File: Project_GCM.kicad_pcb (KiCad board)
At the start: 4 copper layers, 203 x 116 mm, 91 parts, among them IC1 LTC6903CMS8#PBF, J1 Conn_02x04_Odd_Even, J10 Conn_01x10, J11 5530843-2, J12 Conn_02x21_Odd_Even, J13 Conn_01x10, J2 5-5530843-4, J3 5-5530843-4, J4 5-5530843-4, J5 5-5530843-4, J6 TE_Eurocard_96pole, J7 3-641124-6, J8 5530843-2, J9 Conn_01x02, U1 LM810, U10 74LVC1G74, U11 74AHC1G04, U12 74AHC244, U13 SN74LV163A, U14 SN74LV163A, U15 74AHC1G04, U16 SN74LV163A, U17 SN74LV163A, U18 74AHC1G04, U19 SN74LV163A, U2 LTC6994-1, U20 SN74LV163A, U21 74AHC244, U22 74CBTLV16212, U23 74CBTLV16212, U24 74CBTLV16212, U3 74AHC1G32, U4 74AHC273, U5 74AHC1G04, U6 CD74AC238, U7 74AHC138, U8 74AHC244, U9 74AHC244

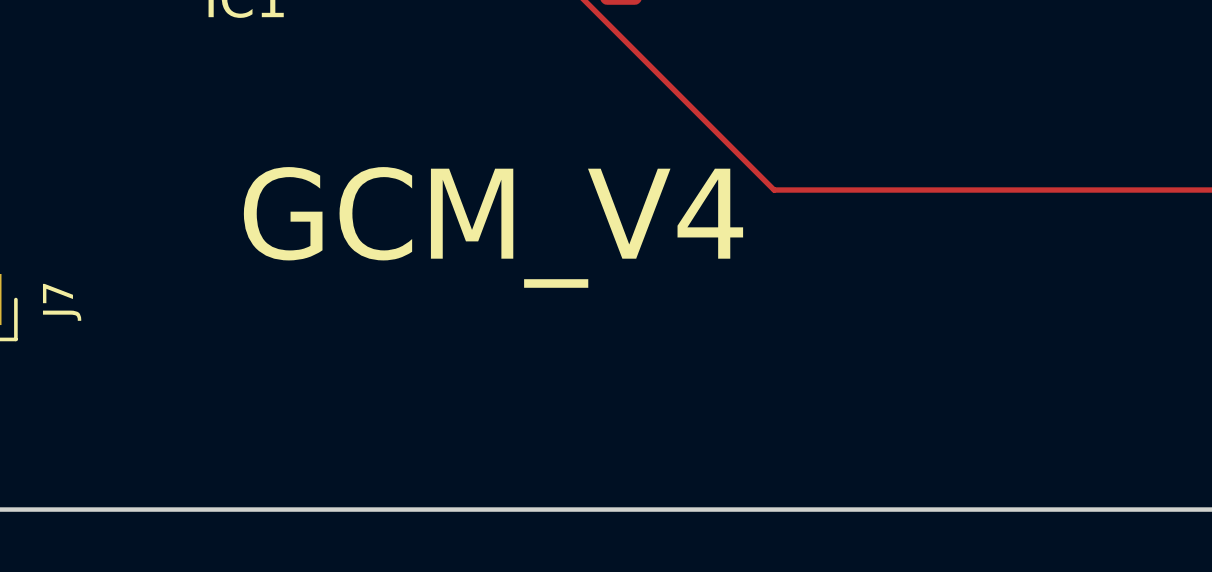
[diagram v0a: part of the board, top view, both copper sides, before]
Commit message: License info on silks
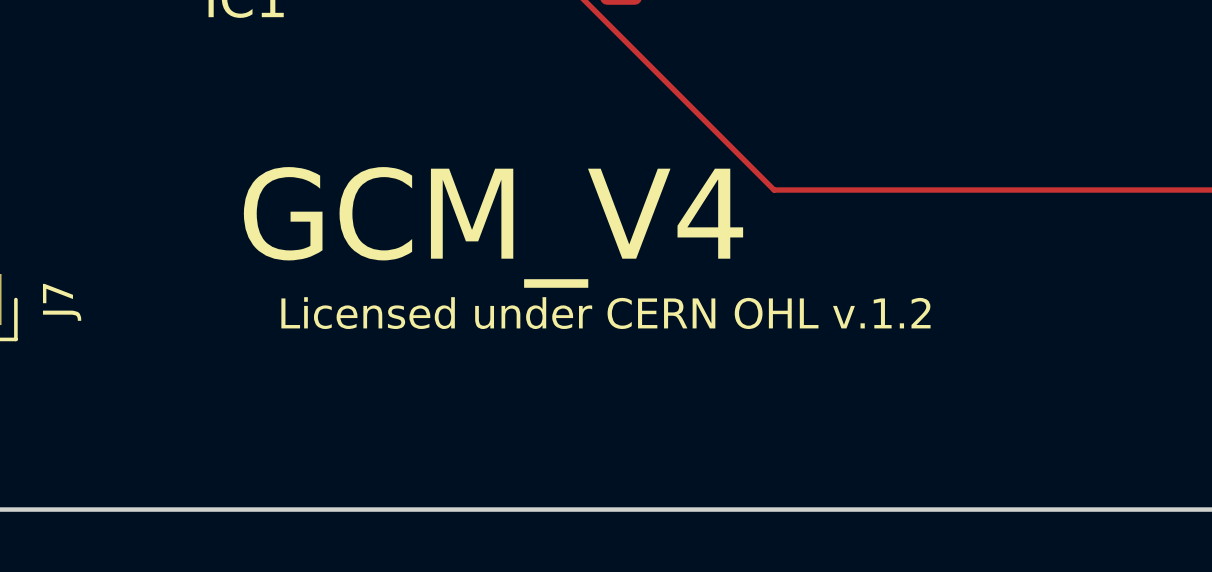
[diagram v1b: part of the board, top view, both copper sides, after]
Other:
- board text added: "Licensed under CERN OHL v.1.2"
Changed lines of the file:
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@@
-(kicad_pcb (version 20171130) (host pcbnew "(5.1.2)-1")
+(kicad_pcb (version 20171130) (host pcbnew "(5.1.4)-1")
   (general
     (thickness 1.6)
-    (drawings 42)
+    (drawings 43)
     (tracks 6223)
     (zones 0)
@@
     )
   )
+  (gr_text "Licensed under CERN OHL v.1.2" (at 167 141.5) (layer F.SilkS)
+    (effects (font (size 1 1) (thickness 0.15)))
+  )
   (gr_line (start 271 32) (end 68 32) (angle 90) (layer Edge.Cuts) (width 0.15))

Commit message: Update materials list, begin to work on pcb
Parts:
- removed IC1: LTC6903CMS8#PBF, SOP65P490X110-8N:SOP65P490X110-8N
- added C35: 10nF, Capacitor_SMD:C_0805_2012Metric, F.Cu at (290.1, 22.9)
- added C36: 10nF, Capacitor_SMD:C_0805_2012Metric, F.Cu at (294.5, 22.9)
- added C37: 10nF, Capacitor_SMD:C_0805_2012Metric, F.Cu at (290.1, 25.9)
- added C38: 10nF, Capacitor_SMD:C_0805_2012Metric, F.Cu at (284.9, 48.5)
- added C39: 10nF, Capacitor_SMD:C_0805_2012Metric, F.Cu at (289.4, 48.5)
- added C40: 10nF, Capacitor_SMD:C_0805_2012Metric, F.Cu at (284.9, 51.5)
- added C41: 10nF, Capacitor_SMD:C_0805_2012Metric, F.Cu at (289.4, 51.5)
- added C49: 10nF, Capacitor_SMD:C_0805_2012Metric, F.Cu at (314.7, 45.6)
- added C50: 10nF, Capacitor_SMD:C_0805_2012Metric, F.Cu at (314.7, 48.6)
- added C51: 10nF, Capacitor_SMD:C_0805_2012Metric, F.Cu at (284.9, 63.9)
- added C52: 10nF, Capacitor_SMD:C_0805_2012Metric, F.Cu at (373.0, 38.2)
- added C53: 10nF, Capacitor_SMD:C_0805_2012Metric, F.Cu at (332.4, 23.0)
- added C54: 10nF, Capacitor_SMD:C_0805_2012Metric, F.Cu at (328.0, 26.0)
- added C55: 10nF, Capacitor_SMD:C_0805_2012Metric, F.Cu at (328.0, 23.0)
- added H1: MountingHole_3mm, MountingHole:MountingHole_3mm, F.Cu at (336.7, 36.4)
- added H2: MountingHole_3mm, MountingHole:MountingHole_3mm, F.Cu at (329.2, 44.0)
- added H3: MountingHole_3mm, MountingHole:MountingHole_3mm, F.Cu at (329.2, 36.4)
- added H4: MountingHole_3mm, MountingHole:MountingHole_3mm, F.Cu at (336.7, 44.0)
- added R6: 10k, Resistor_SMD:R_0805_2012Metric, F.Cu at (294.5, 25.9)
- added U25: 74AHC1G32, Package_TO_SOT_SMD:SOT-23-5, F.Cu at (302.0, 60.2)
- added U26: SN74LV393A, Package_SO:SOIC-14_3.9x8.7mm_P1.27mm, F.Cu at (309.6, 23.7)
- added U27: SN74LV393A, Package_SO:SOIC-14_3.9x8.7mm_P1.27mm, F.Cu at (301.2, 23.7)
- added U28: CD74AC151, Package_SO:SOP-16_3.9x9.9mm_P1.27mm, F.Cu at (301.2, 12.8)
- added U29: CD74AC151, Package_SO:SOP-16_3.9x9.9mm_P1.27mm, F.Cu at (309.8, 12.8)
- added U30: 74AHC1G32, Package_TO_SOT_SMD:SOT-23-5, F.Cu at (285.3, 23.6)
- added U31: CD74AC151, Package_SO:SOP-16_3.9x9.9mm_P1.27mm, F.Cu at (318.3, 12.8)
- added U32: 74AHC273, Package_SO:SOIC-20W_7.5x12.8mm_P1.27mm, F.Cu at (289.2, 39.8)
- added U33: SN74LV393A, Package_SO:SOIC-14_3.9x8.7mm_P1.27mm, F.Cu at (308.3, 49.2)
- added U34: SN74LV393A, Package_SO:SOIC-14_3.9x8.7mm_P1.27mm, F.Cu at (299.8, 49.2)
- added U35: CD74AC151, Package_SO:SOP-16_3.9x9.9mm_P1.27mm, F.Cu at (317.0, 38.4)
- added U36: CD74AC151, Package_SO:SOP-16_3.9x9.9mm_P1.27mm, F.Cu at (308.4, 38.4)
- added U37: CD74AC151, Package_SO:SOP-16_3.9x9.9mm_P1.27mm, F.Cu at (299.9, 38.4)
- added U38: 74AHC1G04, Package_TO_SOT_SMD:SOT-23-5, F.Cu at (290.4, 60.2)
- added U39: 74AHC1G04, Package_TO_SOT_SMD:SOT-23-5, F.Cu at (285.3, 60.2)
- added U40: 74AHC273, Package_SO:SOIC-20W_7.5x12.8mm_P1.27mm, F.Cu at (364.3, 39.5)
- added U41: 74AHC1G04, Package_TO_SOT_SMD:SOT-23-5, F.Cu at (373.4, 34.5)
- added U42: 74AHC273, Package_SO:SOIC-20W_7.5x12.8mm_P1.27mm, F.Cu at (332.2, 14.3)
- added U43: 74AHC273, Package_SO:SOIC-20W_7.5x12.8mm_P1.27mm, F.Cu at (345.1, 14.3)
- added U44: 74AHC273, Package_SO:SOIC-20W_7.5x12.8mm_P1.27mm, F.Cu at (358.0, 14.3)
- added X1: ECS-2200BX-500, Oscillator:Oscillator_DIP-8, F.Cu at (286.0, 18.1)
- C24: value 1uF -> 10nF; footprint Capacitor_SMD:C_1206_3216Metric -> Capacitor_SMD:C_0805_2012Metric
- J1: value Conn_02x04_Odd_Even -> PowerSupply
- J10, J13: value Conn_01x10 -> MM1_addressExtension
- J11, J8: value 5530843-2 -> MM1_receptacle_5530843-2
- J12: value Conn_02x21_Odd_Even -> DEBUG_BUSES
- J2, J3, J4, J5: value 5-5530843-4 -> PP1_receptacle_TE_5-5530843-4; footprint Eurocard:SHDR40W89P485X254_2X20_5740X935X1562P -> TE_5-5530843-4:TE_5-5530843-4
- U1: footprint Package_TO_SOT_SMD:SOT-23_Handsoldering -> Package_TO_SOT_SMD:SOT-23
- U10: footprint Package_SO:VSSOP-8_2.4x2.1mm_P0.5mm -> Package_SO:SSOP-8_2.95x2.8mm_P0.65mm
- U13, U14, U16, U17, U19, U20: value SN74LV163A -> CD74AC161M; footprint Package_SO:SOIC-16_3.9x9.9mm_P1.27mm -> Package_SO:SOP-16_3.9x9.9mm_P1.27mm
- U15: value 74AHC1G04 -> 74AHCT1G04
- U2: value LTC6994-1 -> LTC6994xS6-1; footprint Package_TO_SOT_SMD:SOT-23-6 -> Package_TO_SOT_SMD:TSOT-23-6
- U21: value 74AHC244 -> 74AHCT244
- U6: footprint Package_SO:SOIC-16_3.9x9.9mm_P1.27mm -> Package_SO:SOP-16_3.9x9.9mm_P1.27mm
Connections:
- net /MAIN_RESET renamed /POWER_RESET
- net /MemorySlot1/MEM_ADD_0 renamed /MemorySlot1/MEMADDRESS_0
- net /MemorySlot1/MEM_ADD_1 renamed /MemorySlot1/MEMADDRESS_1
- net /MemorySlot1/MEM_ADD_10 renamed /MemorySlot1/MEMADDRESS_10
- net /MemorySlot1/MEM_ADD_11 renamed /MemorySlot1/MEMADDRESS_11
- net /MemorySlot1/MEM_ADD_12 renamed /MemorySlot1/MEMADDRESS_12
- net /MemorySlot1/MEM_ADD_13 renamed /MemorySlot1/MEMADDRESS_13
- net /MemorySlot1/MEM_ADD_14 renamed /MemorySlot1/MEMADDRESS_14
- net /MemorySlot1/MEM_ADD_15 renamed /MemorySlot1/MEMADDRESS_15
- net /MemorySlot1/MEM_ADD_16 renamed /MemorySlot1/MEMADDRESS_16
- net /MemorySlot1/MEM_ADD_17 renamed /MemorySlot1/MEMADDRESS_17
- net /MemorySlot1/MEM_ADD_18 renamed /MemorySlot1/MEMADDRESS_18
- net /MemorySlot1/MEM_ADD_19 renamed /MemorySlot1/MEMADDRESS_19
- net /MemorySlot1/MEM_ADD_2 renamed /MemorySlot1/MEMADDRESS_2
- net /MemorySlot1/MEM_ADD_20 renamed /MemorySlot1/MEMADDRESS_20
- net /MemorySlot1/MEM_ADD_21 renamed /MemorySlot1/MEMADDRESS_21
- net /MemorySlot1/MEM_ADD_22 renamed /MemorySlot1/MEMADDRESS_22
- net /MemorySlot1/MEM_ADD_23 renamed /MemorySlot1/MEMADDRESS_23
- net /MemorySlot1/MEM_ADD_3 renamed /MemorySlot1/MEMADDRESS_3
- net /MemorySlot1/MEM_ADD_4 renamed /MemorySlot1/MEMADDRESS_4
- net /MemorySlot1/MEM_ADD_5 renamed /MemorySlot1/MEMADDRESS_5
- net /MemorySlot1/MEM_ADD_6 renamed /MemorySlot1/MEMADDRESS_6
- net /MemorySlot1/MEM_ADD_7 renamed /MemorySlot1/MEMADDRESS_7
- net /MemorySlot1/MEM_ADD_8 renamed /MemorySlot1/MEMADDRESS_8
- net /MemorySlot1/MEM_ADD_9 renamed /MemorySlot1/MEMADDRESS_9
- net /MemorySlot1/MEM_FEEDBACK renamed /MemorySlot1/MEMFEEDBACK
- net /MemorySlot2/MEM_ADD_0 renamed /MemorySlot2/MEMADDRESS_0
- net /MemorySlot2/MEM_ADD_1 renamed /MemorySlot2/MEMADDRESS_1
- net /MemorySlot2/MEM_ADD_10 renamed /MemorySlot2/MEMADDRESS_10
- net /MemorySlot2/MEM_ADD_11 renamed /MemorySlot2/MEMADDRESS_11
- net /MemorySlot2/MEM_ADD_12 renamed /MemorySlot2/MEMADDRESS_12
- net /MemorySlot2/MEM_ADD_13 renamed /MemorySlot2/MEMADDRESS_13
- net /MemorySlot2/MEM_ADD_14 renamed /MemorySlot2/MEMADDRESS_14
- net /MemorySlot2/MEM_ADD_15 renamed /MemorySlot2/MEMADDRESS_15
- net /MemorySlot2/MEM_ADD_16 renamed /MemorySlot2/MEMADDRESS_16
- net /MemorySlot2/MEM_ADD_17 renamed /MemorySlot2/MEMADDRESS_17
- net /MemorySlot2/MEM_ADD_18 renamed /MemorySlot2/MEMADDRESS_18
- net /MemorySlot2/MEM_ADD_19 renamed /MemorySlot2/MEMADDRESS_19
- net /MemorySlot2/MEM_ADD_2 renamed /MemorySlot2/MEMADDRESS_2
- net /MemorySlot2/MEM_ADD_20 renamed /MemorySlot2/MEMADDRESS_20
- net /MemorySlot2/MEM_ADD_21 renamed /MemorySlot2/MEMADDRESS_21
- net /MemorySlot2/MEM_ADD_22 renamed /MemorySlot2/MEMADDRESS_22
- net /MemorySlot2/MEM_ADD_23 renamed /MemorySlot2/MEMADDRESS_23
- net /MemorySlot2/MEM_ADD_3 renamed /MemorySlot2/MEMADDRESS_3
- net /MemorySlot2/MEM_ADD_4 renamed /MemorySlot2/MEMADDRESS_4
- net /MemorySlot2/MEM_ADD_5 renamed /MemorySlot2/MEMADDRESS_5
- net /MemorySlot2/MEM_ADD_6 renamed /MemorySlot2/MEMADDRESS_6
- net /MemorySlot2/MEM_ADD_7 renamed /MemorySlot2/MEMADDRESS_7
- net /MemorySlot2/MEM_ADD_8 renamed /MemorySlot2/MEMADDRESS_8
- net /MemorySlot2/MEM_ADD_9 renamed /MemorySlot2/MEMADDRESS_9
- net /MemorySlot2/MEM_FEEDBACK renamed /MemorySlot2/MEMFEEDBACK
- net /RESET_CLK renamed /GLOBAL_RESET
- net /SOURCE_RESET renamed /LIGHT_RESET
- net /~GLOBAL_CLK renamed /AddressCounter/ADDSRC_DELAYED_CLK
- C11 pad 1: GND -> +5V
- C11 pad 2: +5V -> GND
- C17 pad 1: +5V -> GND
- C17 pad 2: GND -> +3V3
- C18 pad 1: +5V -> GND
- C18 pad 2: GND -> +3V3
- C19 pad 1: +5V -> GND
- C19 pad 2: GND -> +3V3
- C20 pad 1: +5V -> GND
- C20 pad 2: GND -> +3V3
- C21 pad 1: +5V -> GND
- C21 pad 2: GND -> +3V3
- C22 pad 1: +5V -> GND
- C22 pad 2: GND -> +3V3
- C23 pad 2: +5V -> +3V3
- C28 pad 2: +5V -> +3V3
- C4 pad 1: +5V -> GND
- C4 pad 2: GND -> +5V
- J2 pad 3: /GLOBAL_CLK -> /P_CLK
- J2 pad 5: /~RESET_CLK -> /~GLOBAL_RESET
- J3 pad 3: /GLOBAL_CLK -> /P_CLK
- J3 pad 5: /~RESET_CLK -> /~GLOBAL_RESET
- J4 pad 3: /GLOBAL_CLK -> /P_CLK
- J4 pad 5: /~RESET_CLK -> /~GLOBAL_RESET
- J5 pad 3: /GLOBAL_CLK -> /P_CLK
- J5 pad 5: /~RESET_CLK -> /~GLOBAL_RESET
- U10 pad 1: /CLK_MODULE_5 -> /CLK_MODULE_6
- U10 pad 6: /~MAIN_RESET -> /~POWER_RESET
- U10 pad 7: +5V -> +3V3
- U10 pad 8: +5V -> +3V3
- U11 pad 4: /~MAIN_RESET -> /~POWER_RESET
- U12 pad 1: /~CS_MODULE_6 -> /MemoryController/USER_OE
- U12 pad 19: /~CS_MODULE_6 -> /MemoryController/USER_OE
- U12 pad 20: +5V -> +3V3
- U13 pad 1: /~RESET_CLK -> /~GLOBAL_RESET
- U13 pad 10: +5V -> +3V3
- U13 pad 16: +5V -> +3V3
- U13 pad 7: /ADDSRC_CLK -> +3V3
- U14 pad 1: /~RESET_CLK -> /~GLOBAL_RESET
- U14 pad 16: +5V -> +3V3
- U14 pad 7: /ADDSRC_CLK -> +3V3
- U15 pad 2: /CLK_MODULE_6 -> /MemoryController/USER_~OE
- U15 pad 4: /MemoryController/~MEMWRITE_CLK -> /MemoryController/USER_OE
- U16 pad 1: /~RESET_CLK -> /~GLOBAL_RESET
- U16 pad 16: +5V -> +3V3
- U16 pad 7: /ADDSRC_CLK -> +3V3
- U17 pad 1: /~RESET_CLK -> /~GLOBAL_RESET
- U17 pad 16: +5V -> +3V3
- U17 pad 7: /ADDSRC_CLK -> +3V3
- U19 pad 1: /~RESET_CLK -> /~GLOBAL_RESET
- U19 pad 16: +5V -> +3V3
- U19 pad 7: /ADDSRC_CLK -> +3V3
- U2 pad 1: /CLK_MODULE_5 -> /LIGHT_RESET_IN
- U20 pad 1: /~RESET_CLK -> /~GLOBAL_RESET
- U20 pad 16: +5V -> +3V3
- U20 pad 7: /ADDSRC_CLK -> +3V3
- U22 pad 22: GND -> /MemoryController/USER_~CE
- U22 pad 23: +5V -> +3V3
- U22 pad 24: /MemoryController/~MEMWRITE_CLK -> /MemoryController/USER_~WE
- U22 pad 26: /~CS_MODULE_5 -> /MemoryController/USER_~OE
- U23 pad 10: /AddressCounter/BJMPSRC_3 -> /MemoryController/AddressExchanger/USERADDRESS_3
- U23 pad 12: /AddressCounter/BJMPSRC_4 -> /MemoryController/AddressExchanger/USERADDRESS_4
- U23 pad 14: /AddressCounter/BJMPSRC_5 -> /MemoryController/AddressExchanger/USERADDRESS_5
- U23 pad 16: /AddressCounter/BJMPSRC_6 -> /MemoryController/AddressExchanger/USERADDRESS_6
- U23 pad 20: /AddressCounter/BJMPSRC_7 -> /MemoryController/AddressExchanger/USERADDRESS_7
- U23 pad 22: /AddressCounter/BJMPSRC_8 -> /MemoryController/AddressExchanger/USERADDRESS_8
- U23 pad 24: /AddressCounter/BJMPSRC_9 -> /MemoryController/AddressExchanger/USERADDRESS_9
- U23 pad 26: /AddressCounter/BJMPSRC_10 -> /MemoryController/AddressExchanger/USERADDRESS_10
- U23 pad 28: /AddressCounter/BJMPSRC_11 -> /MemoryController/AddressExchanger/USERADDRESS_11
- U23 pad 3: /AddressCounter/BJMPSRC_0 -> /MemoryController/AddressExchanger/USERADDRESS_0
- U23 pad 5: /AddressCounter/BJMPSRC_1 -> /MemoryController/AddressExchanger/USERADDRESS_1
- U23 pad 7: /AddressCounter/BJMPSRC_2 -> /MemoryController/AddressExchanger/USERADDRESS_2
- U24 pad 10: /AddressCounter/BJMPSRC_15 -> /MemoryController/AddressExchanger/USERADDRESS_15
- U24 pad 12: /AddressCounter/BJMPSRC_16 -> /MemoryController/AddressExchanger/USERADDRESS_16
- U24 pad 14: /AddressCounter/BJMPSRC_17 -> /MemoryController/AddressExchanger/USERADDRESS_17
- U24 pad 16: /AddressCounter/BJMPSRC_18 -> /MemoryController/AddressExchanger/USERADDRESS_18
- U24 pad 20: /AddressCounter/BJMPSRC_19 -> /MemoryController/AddressExchanger/USERADDRESS_19
- U24 pad 22: /AddressCounter/BJMPSRC_20 -> /MemoryController/AddressExchanger/USERADDRESS_20
- U24 pad 24: /AddressCounter/BJMPSRC_21 -> /MemoryController/AddressExchanger/USERADDRESS_21
- U24 pad 26: /AddressCounter/BJMPSRC_22 -> /MemoryController/AddressExchanger/USERADDRESS_22
- U24 pad 28: /AddressCounter/BJMPSRC_23 -> /MemoryController/AddressExchanger/USERADDRESS_23
- U24 pad 3: /AddressCounter/BJMPSRC_12 -> /MemoryController/AddressExchanger/USERADDRESS_12
- U24 pad 5: /AddressCounter/BJMPSRC_13 -> /MemoryController/AddressExchanger/USERADDRESS_13
- U24 pad 7: /AddressCounter/BJMPSRC_14 -> /MemoryController/AddressExchanger/USERADDRESS_14
- U4 pad 1: /~RESET_CLK -> /~POWER_RESET
- U4 pad 12: Net-(U4-Pad12) -> /ClockGenerator/CLK_SELECT_SLOW_1
- U4 pad 13: GND -> /ClockGenerator/BWRITE1_4
- U4 pad 14: GND -> /ClockGenerator/BWRITE1_5
- U4 pad 15: Net-(U4-Pad15) -> /ClockGenerator/CLK_SELECT_SLOW_2
- U4 pad 16: Net-(U4-Pad16) -> /ClockGenerator/CLK_SELECT_0
- U4 pad 17: GND -> /ClockGenerator/BWRITE1_6
- U4 pad 18: GND -> /ClockGenerator/BWRITE1_7
- U4 pad 19: Net-(U4-Pad19) -> /ClockGenerator/CLK_SELECT_1
- U4 pad 2: /ClockGenerator/CLK_SDI -> /ClockGenerator/CLK_SELECT_FAST_0
- U4 pad 5: /ClockGenerator/CLK_SCK -> /ClockGenerator/CLK_SELECT_FAST_1
- U4 pad 6: /ClockGenerator/CLK_~SEN -> /ClockGenerator/CLK_SELECT_FAST_2
- U4 pad 8: GND -> /ClockGenerator/BWRITE1_3
- U4 pad 9: Net-(U4-Pad9) -> /ClockGenerator/CLK_SELECT_SLOW_0
- U5 pad 4: /~RESET_CLK -> /~GLOBAL_RESET
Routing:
- net GND: track 1212.4 -> 0.00 mm, vias 13 -> 0
- net +5V: track 724.3 -> 0.00 mm, vias 12 -> 0
- net +3V3: track 384.5 -> 0.00 mm, vias 9 -> 0
- net /Connector/BREAD2_7: track 316.3 -> 0.00 mm, vias 1 -> 0
- net /~RESET_CLK: track 277.3 -> 0.00 mm, vias 4 -> 0
- net /Connector/BREAD2_6: track 262.6 -> 0.00 mm, vias 1 -> 0
- net /Connector/BREAD2_4: track 248.4 -> 0.00 mm, vias 1 -> 0
- net /Connector/BREAD2_5: track 244.4 -> 0.00 mm, vias 2 -> 0
- net /Connector/BWRITE2_7: track 237.6 -> 0.00 mm, vias 1 -> 0
- net /ClockGenerator/BWRITE1_0: track 237.5 -> 0.00 mm, vias 4 -> 0
- net /Connector/BREAD2_3: track 234.9 -> 0.00 mm, vias 2 -> 0
- net /Connector/BWRITE2_6: track 234.4 -> 0.00 mm, vias 2 -> 0
- net /ClockGenerator/BWRITE1_7: track 229.3 -> 0.00 mm, vias 4 -> 0
- net /Connector/BREAD2_2: track 227.0 -> 0.00 mm, vias 2 -> 0
- net /GLOBAL_CLK: track 224.2 -> 0.00 mm, vias 3 -> 0
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
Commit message: First pass on the PCB
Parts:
- removed HOLE1, HOLE2, HOLE3, HOLE4: MountingHole_3mm, Mounting_Holes:MountingHole_3mm
- C11, C12, C13, C28, C29, C31, C52, C7, C8, R6, U11, U12, U15, U21, U23, U3, U40, U41, U5, U6, U7, U8, U9: moved to B.Cu
- C6, U18, U4: moved to F.Cu
- J10, J13: footprint Connector_Multicomp:Multicomp_MC9A12-1034_2x05_P2.54mm_Vertical -> Connector_IDC:IDC-Header_2x05_P2.54mm_Vertical
- moved H3 277.5 mm to (73.0, 143.0)
- moved H1 263.7 mm to (73.0, 37.0)
- moved C52 254.2 mm to (129.0, 109.5), turned to 180 degrees
- moved U40 244.6 mm to (132.7, 118.0), turned to 180 degrees
- moved U41 241.7 mm to (145.0, 113.5)
- moved U44 224.7 mm to (158.5, 117.8)
- moved U43 224.7 mm to (145.6, 117.8)
- moved U42 224.7 mm to (132.7, 117.8)
- moved C53 214.6 mm to (136.0, 109.5)
- moved C54 197.5 mm to (149.0, 109.5)
- moved C55 187.2 mm to (162.0, 109.5)
- moved U26 178.2 mm to (135.0, 59.0)
- moved U27 173.2 mm to (135.0, 72.5)
- moved U29 173.1 mm to (147.5, 73.0)
- moved U31 167.3 mm to (159.5, 65.5)
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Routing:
- net GND: track 0.00 -> 1456.1 mm, vias 0 -> 15
- net +5V: track 0.00 -> 789.9 mm, vias 0 -> 12
- net +3V3: track 0.00 -> 532.6 mm, vias 0 -> 7
- net /ClockGenerator/BWRITE1_5: track 0.00 -> 329.4 mm, vias 0 -> 5
- net /ClockGenerator/BWRITE1_0: track 0.00 -> 326.1 mm, vias 0 -> 6
- net /ClockGenerator/BWRITE1_4: track 0.00 -> 323.8 mm, vias 0 -> 5
- net /ClockGenerator/BWRITE1_1: track 0.00 -> 309.6 mm, vias 0 -> 4
- net /ClockGenerator/BWRITE1_2: track 0.00 -> 309.0 mm, vias 0 -> 4
- net /Connector/BWRITE2_4: track 0.00 -> 302.5 mm, vias 0 -> 4
- net /ClockGenerator/BWRITE1_3: track 0.00 -> 300.6 mm, vias 0 -> 5
- net /Connector/BWRITE2_0: track 0.00 -> 299.3 mm, vias 0 -> 5
- net /Connector/BWRITE2_2: track 0.00 -> 295.4 mm, vias 0 -> 4
- net /Connector/BWRITE2_5: track 0.00 -> 294.0 mm, vias 0 -> 5
- net /Connector/BWRITE2_1: track 0.00 -> 289.8 mm, vias 0 -> 3
- net /Connector/BWRITE2_3: track 0.00 -> 285.9 mm, vias 0 -> 3
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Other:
- net class Volt: trace_width 0.3 -> 0.25
- board text added: "GCM_V5"
- board text added: "Licensed under CERN-OHL-W v2 or later"
- board text removed: "GCM_V4"
- board text removed: "Licensed under CERN OHL v.1.2"

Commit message: Second pass on pcb
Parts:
- moved C14 1.50 mm to (129.5, 139.5)
- moved J7 1.50 mm to (146.0, 139.5)
- moved R5 1.50 mm to (136.0, 135.5)
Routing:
- net GND: track 1456.1 -> 1475.7 mm
- net +3V3: track 532.6 -> 535.7 mm
- net /AddressCounter/~JMPSRC_CLK: track 85.6 -> 87.2 mm
- net /SPI_MOSI: track 116.1 -> 114.6 mm
- net /SPI_MISO: track 124.7 -> 123.5 mm
- net /MemoryController/USER_RW_2: track 100.7 -> 101.8 mm
- net /ClockGenerator/PClockGenerator/CLK_SELECT_1: track 42.0 -> 42.8 mm
- net /FREQUENCY_SWITCH_SIGNAL: track 16.4 -> 17.2 mm
- net +5V: track 789.9 -> 790.6 mm
- net /ClockGenerator/BWRITE1_5: track 329.4 -> 330.1 mm
- net /SPI_SCLK: track 121.7 -> 121.0 mm
- net /~POWER_RESET: track 208.2 -> 208.9 mm
- net /ClockGenerator/BWRITE1_0: track 326.1 -> 326.7 mm
- net /BDATASRC_0: track 159.9 -> 159.3 mm
- net Net-(U13-Pad15): track 16.0 -> 16.5 mm
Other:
- board text added: "Debug buses"
- board text added: "GCM - V5.0"
- board text added: "MM1 slot 1"
- board text added: "MM1 slot 1 address extension"
- board text added: "MM1 slot 2"
- board text added: "MM1 slot 2 address extension"
- board text added: "MOM1_SPS1"
- board text added: "PP1 receptacle"
- board text added: "Power supply"
- board text added: "pause"
- board text removed: "Debug info"
- board text removed: "GCM_V5"
- board text removed: "MEM1"
- board text removed: "MEM1 Address Extension"
- board text removed: "MEM2"
- board text removed: "MEM2 Address Extension"
